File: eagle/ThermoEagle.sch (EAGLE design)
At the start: 30 parts, among them IC1 MAX232, IC2 4511N, Q1 20MHz, T1 2N2219, T2 2N2219, U1 LM324

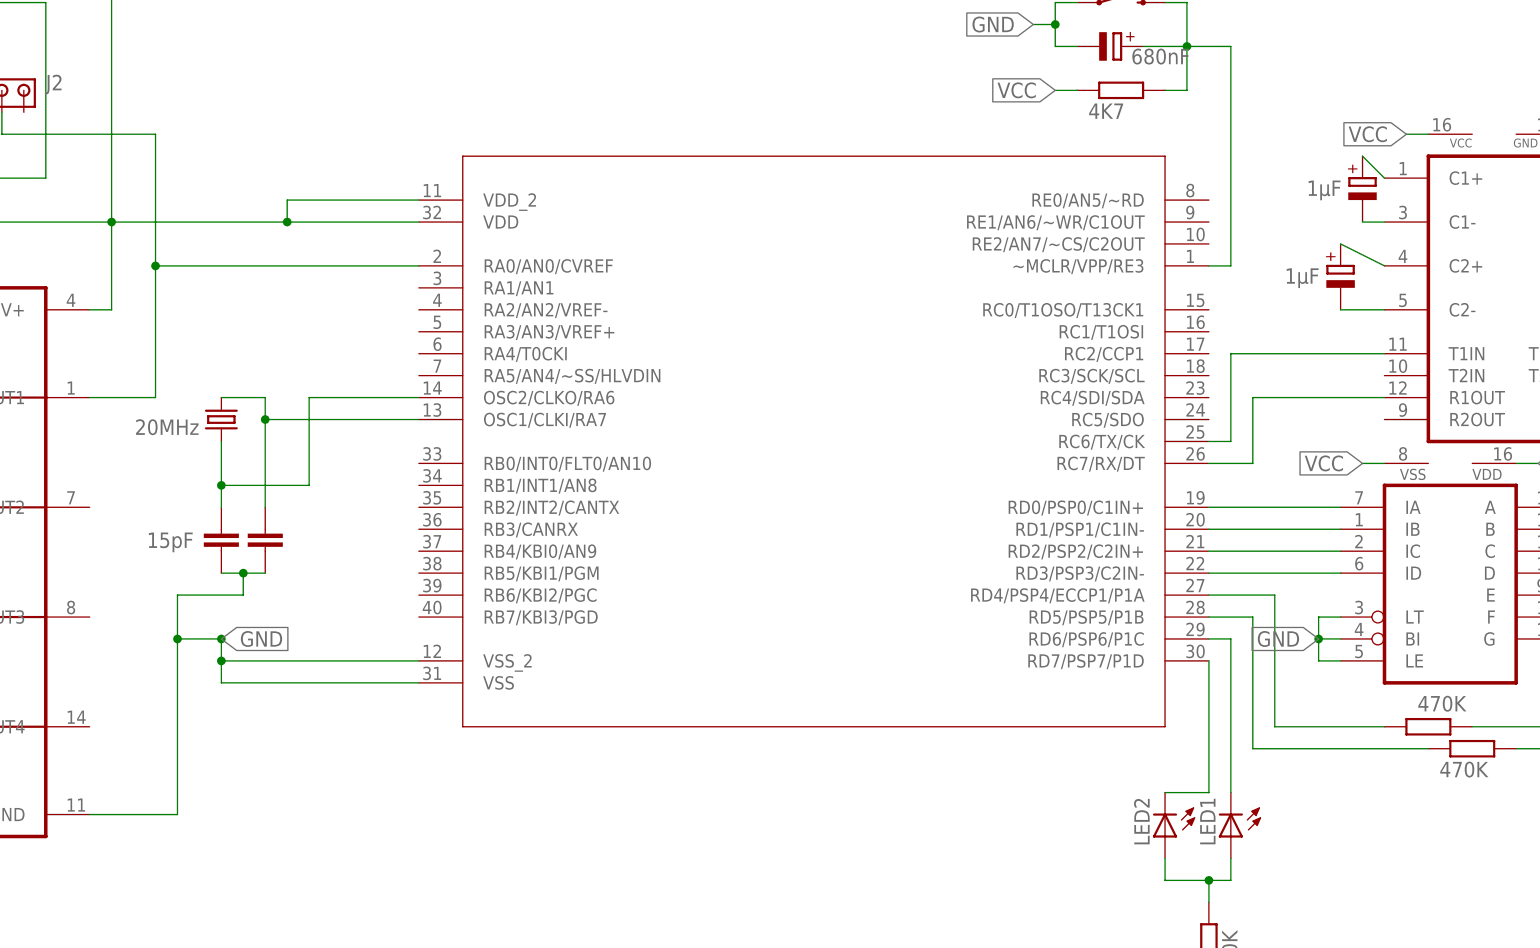
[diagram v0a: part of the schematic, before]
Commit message: connector
ajout des connecteurs, pour les parties non connectées
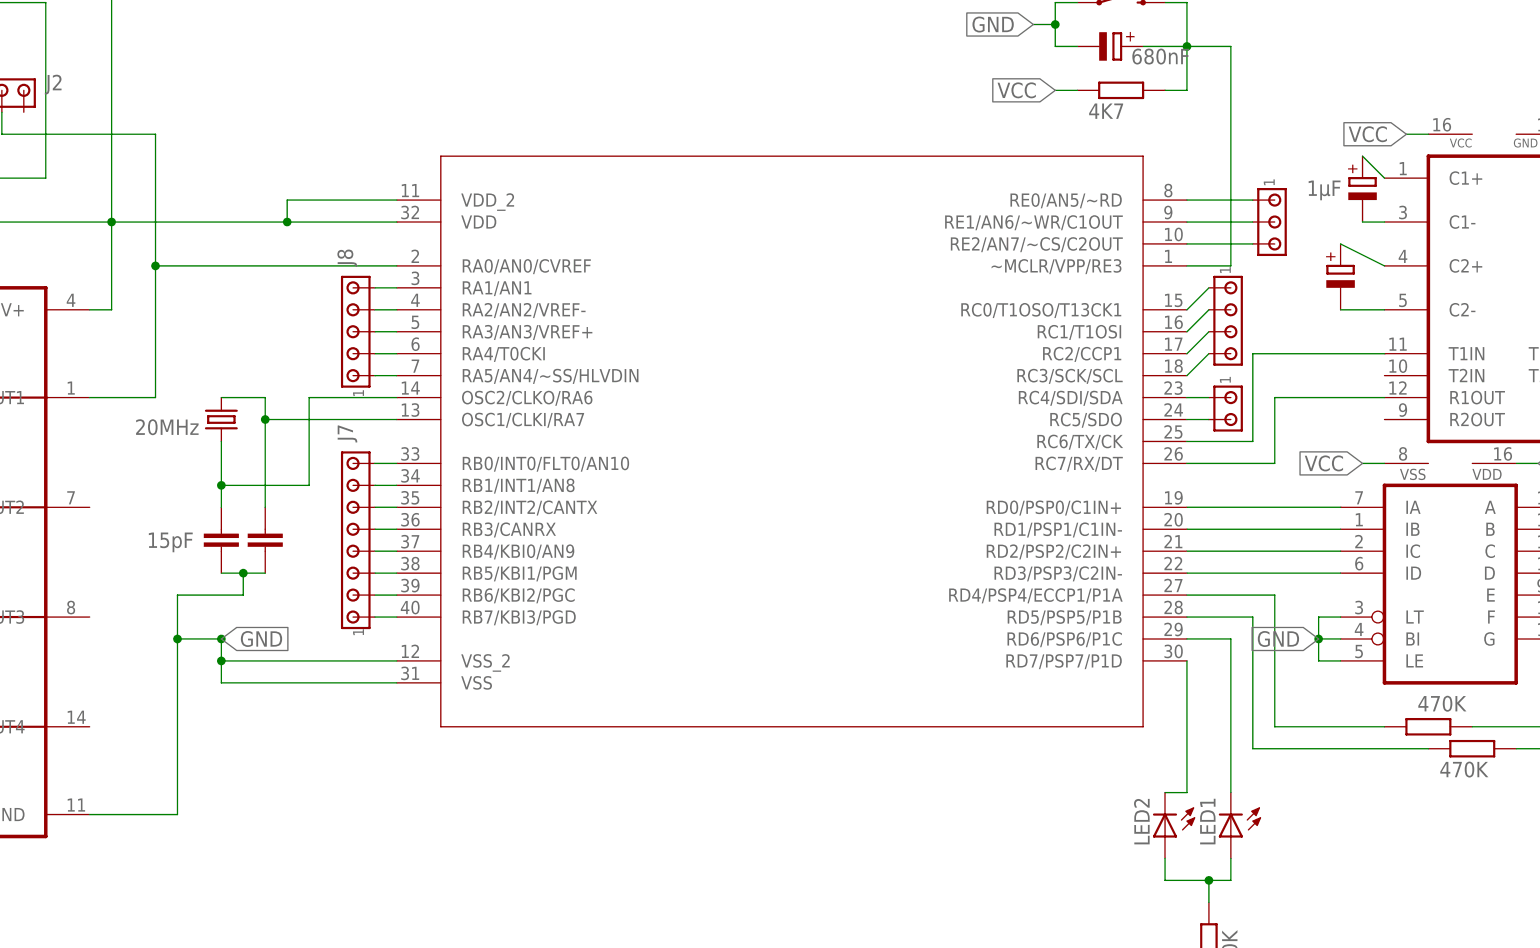
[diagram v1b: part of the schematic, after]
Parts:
- added J1: (no value), con-amp:MTA04-100
- added J3: (no value), con-amp:MTA02-100
- added J4: (no value), con-amp:MTA03-100
- added J7: (no value), con-amp:MTA08-100
- added J8: (no value), con-amp:MTA05-100
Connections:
- new net N$32: J8.5, U$1.RA1/AN1
- new net N$33: J8.4, U$1.RA2/AN2/VREF-
- new net N$34: J8.3, U$1.RA3/AN3/VREF+
- new net N$35: J8.2, U$1.RA4/T0CKI
- new net N$47: J8.1, U$1.RA5/AN4/~SS/HLVDIN
- new net N$50: J7.8, U$1.RB0/INT0/FLT0/AN10
- new net N$51: J7.7, U$1.RB1/INT1/AN8
- new net N$54: J7.6, U$1.RB2/INT2/CANTX
- new net N$58: J7.5, U$1.RB3/CANRX
- new net N$59: J7.4, U$1.RB4/KBI0/AN9
- new net N$60: J7.3, U$1.RB5/KBI1/PGM
- new net N$61: J7.2, U$1.RB6/KBI2/PGC
- new net N$62: J7.1, U$1.RB7/KBI3/PGD
- new net N$63: J4.1, U$1.RE0/AN5/~RD
- new net N$64: J4.2, U$1.RE1/AN6/~WR/C1OUT
- new net N$65: J4.3, U$1.RE2/AN7/~CS/C2OUT
- new net N$66: J1.1, U$1.RC0/T1OSO/T13CK1
- new net N$67: J1.2, U$1.RC1/T1OSI
- new net N$68: J1.3, U$1.RC2/CCP1
- new net N$69: J1.4, U$1.RC3/SCK/SCL
- new net N$70: J3.1, U$1.RC4/SDI/SDA
- new net N$71: J3.2, U$1.RC5/SDO

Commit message: Erreur corrigé
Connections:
- removed net N$5: IC2A.BI, IC2A.LE, IC2A.LT
- new net N$55: IC2A.LE
- new net N$73: IC2A.BI, IC2A.LT
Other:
- moved on the sheet: LED1, LED2

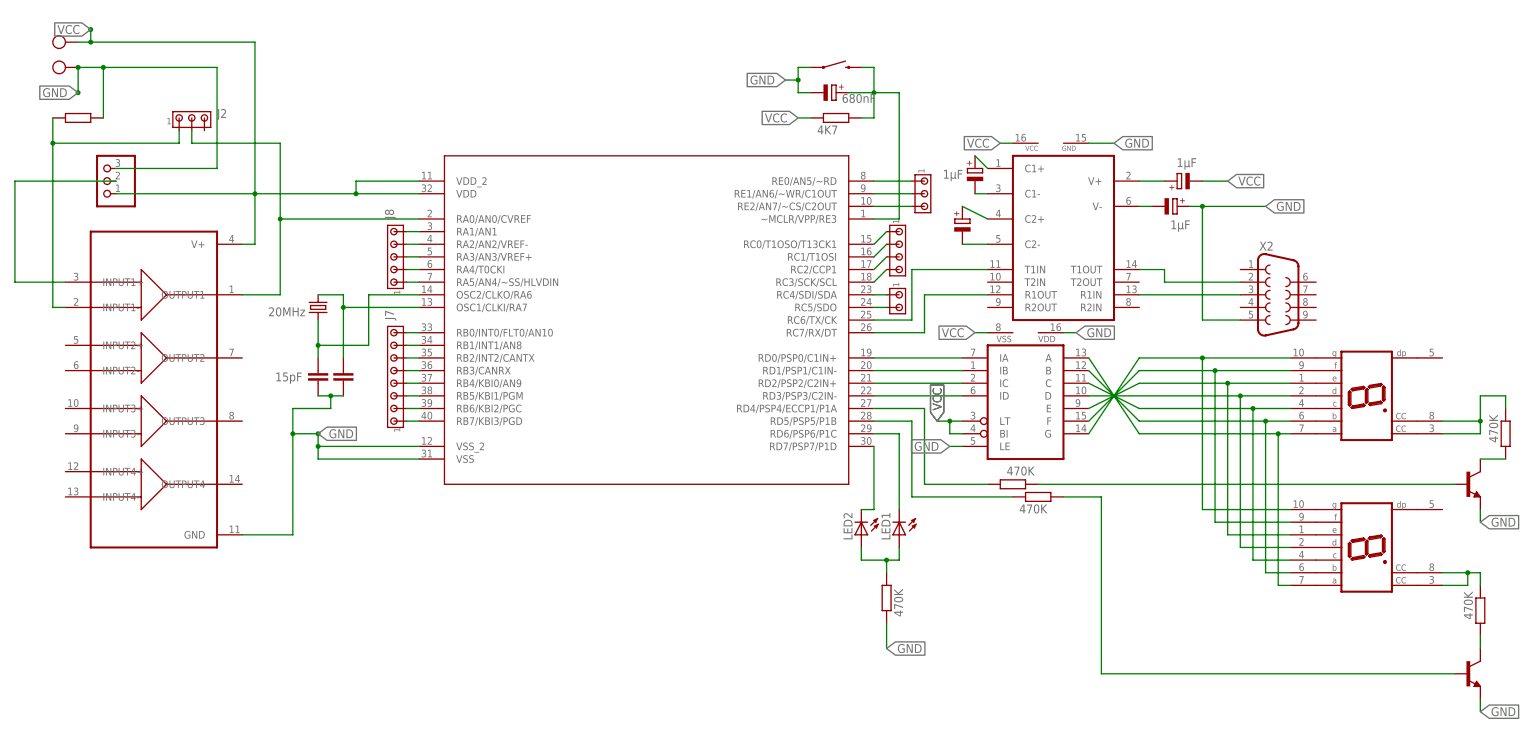
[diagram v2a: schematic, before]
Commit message: Update Eagle files (schema + board)
I hope this time it's the final update.
- Added GND and VCC labels for componenets Maxime had forgotten,
- Updated board with new routes, etc.
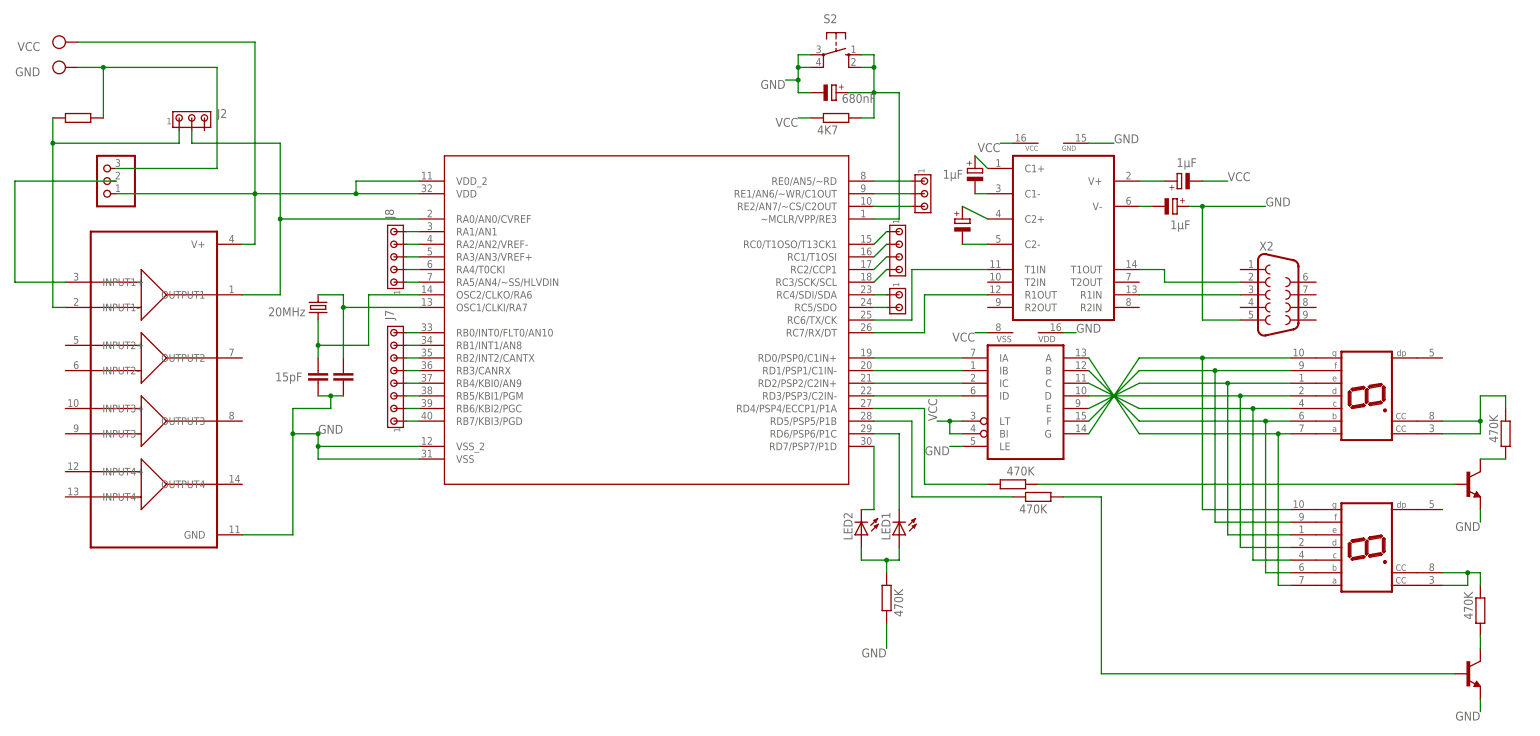
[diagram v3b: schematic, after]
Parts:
- removed S1: MOMENTARY-SWITCH-SPST-PTH-6.0MM, SparkFun-Switches:MOMENTARY-SWITCH-SPST-PTH-6.0MM
- added S2: (no value), DC_LOAD_AU:10-XX
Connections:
- removed net N$18: C2.-
- removed net N$20: C3.+, X2.5
- removed net N$29: T1.E
- removed net N$39: IC1P.VCC
- removed net N$40: IC1P.GND
- removed net N$42: IC2P.VSS
- removed net N$43: IC2P.VDD
- removed net N$46: R1.1
- removed net N$55: IC2A.LE
- removed net N$56: C8.-, S1.1
- removed net N$57: R14.1
- removed net N$73: IC2A.BI, IC2A.LT
- removed net N$8: T2.E
- net GND: now also C3.+, C8.-, IC1P.GND, IC2A.LE, IC2P.VDD, R1.1, S2.P, S2.P1, T1.E, T2.E, X2.5
- net N$72: now also S2.S, S2.S1; no longer S1.2
- net VCC: now also C2.-, IC1P.VCC, IC2A.BI, IC2A.LT, IC2P.VSS, R14.1
